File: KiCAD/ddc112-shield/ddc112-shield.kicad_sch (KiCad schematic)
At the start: 24 parts, among them J1 Power, J2 Digital/PWM, J3 Analog, J4 Digital/PWM, J5 Conn_02x03_Odd_Even, U2 REF3040, U3 OPA350, Y1 10MHZ

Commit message: working on schematic
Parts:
- removed C7: 0.1uF, symbol Device:C_Small
- removed Y1: 10MHZ, Oscillator:Oscillator_DIP-8, symbol Oscillator:CXO_DIP8
- added JP1: JPR2, symbol Jumper:Jumper_2_Bridged
- added R5, R6: 10k, symbol Device:R_US
- added U4, U5: 74AHC1G86, symbol 74xGxx:74AHC1G86
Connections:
- net *9: no longer J2.9 (Pin_9)
- net GND: now also U4.3 (GND), U5.3 (GND)
- net VCC: now also U4.5 (VCC), U5.5 (VCC)
- net at U1.10 (CLK): now also U4.4
- net at U1.9 (CONV): now also U5.4
- net *6 renamed OC0A/6
- net OC0A/6: now also U4.1
- new net: R6.2, U4.2
- new net: R5.2, U5.2
- new net OC1A/9: J2.9 (Pin_9), U5.1

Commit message: initial schematic; test software
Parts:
- removed J5: Conn_02x03_Odd_Even, symbol Connector_Generic:Conn_02x03_Odd_Even
- removed JP1: JPR2, symbol Jumper:Jumper_2_Bridged
- removed R3, R4, R5, R6: 10k, symbol Device:R_US
- removed U4, U5: 74AHC1G86, symbol 74xGxx:74AHC1G86
- added C12, C13: 0.33uF, Capacitor_SMD:C_0805_2012Metric_Pad1.18x1.45mm_HandSolder, symbol Device:C_Small
- added C14, C7: 0.1uF, Capacitor_SMD:C_0805_2012Metric_Pad1.18x1.45mm_HandSolder, symbol Device:C_Small
- added J5, J6: Conn_01x02, Connector_PinHeader_2.54mm:PinHeader_1x02_P2.54mm_Vertical, symbol Connector_Generic:Conn_01x02
- added J7: Screw_Terminal_01x02, TerminalBlock:TerminalBlock_MaiXu_MX126-5.0-02P_1x02_P5.00mm, symbol Connector:Screw_Terminal_01x02
- added U4, U5: L78L05_SOT89, Package_TO_SOT_SMD:SOT-89-3, symbol Regulator_Linear:L78L05_SOT89
- C1, C10, C11, C2, C3, C4, C5, C6, C8, C9: footprint (none) -> Capacitor_SMD:C_0805_2012Metric_Pad1.18x1.45mm_HandSolder
- R1: footprint (none) -> Resistor_SMD:R_0805_2012Metric_Pad1.20x1.40mm_HandSolder
- R2: value 10k -> 0R; footprint (none) -> Resistor_SMD:R_0805_2012Metric_Pad1.20x1.40mm_HandSolder
- U1: value ~ -> DDC112; footprint (none) -> Package_SO:SOIC-28W_7.5x17.9mm_P1.27mm
- U3: footprint (none) -> Package_SO:SOIC-8_3.9x4.9mm_P1.27mm
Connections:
- net *5 is gone; now on net PD5: J4.3 (Pin_3)
- net 7 is gone; now on net PD7: J4.1 (Pin_1)
- net A0 is gone; now on net PC0/ADC0: J3.1 (Pin_1)
- net A1 is gone; now on net PC1/ADC1: J3.2 (Pin_2)
- net A2 is gone; now on net PC2/ADC2: J3.3 (Pin_3)
- net OC0A/6 is gone; now on net PD6/OC0A: J4.2 (Pin_2)
- net OC1A/9 is gone; now on net PB1/OC1A: J2.9 (Pin_9)
- net +5VA: now also C7.1, U4.1 (OUT)
- net Earth: now also R2.2, C12.2, C7.2, J5.2 (Pin_2), J6.2 (Pin_2), U4.2 (GND)
- net GND: now also R2.1, C13.2, C14.2, J7.2 (Pin_2), U5.2 (GND)
- net MISO/12: no longer J2.6 (Pin_6)
- net MOSI/11: no longer J2.7 (Pin_7)
- net VCC: now also C14.1, U5.1 (OUT); no longer J1.8 (Pin_8), R2.2
- net PC1/ADC1: now reaches U1.19 (RANGE1)
- net PC2/ADC2: now reaches U1.20 (RANGE2)
- net PC0/ADC0: now reaches U1.18 (RANGE0)
- net PC0/ADC0: no longer R2.1
- net at U1.1 (IN1): now also J5.1 (Pin_1)
- net PD6/OC0A: now reaches U1.10 (CLK)
- net at U1.28 (IN2): now also J6.1 (Pin_1)
- net PD5: now reaches U1.8 (TEST)
- net PB1/OC1A: now reaches U1.9 (CONV)
- net *3 renamed PD3
- net *9 renamed PD7
- net 2 renamed PD2
- net 4 renamed PD4
- net 8 renamed PB0
- net PB0: now also U1.12 (~{DXMIT})
- net A3 renamed PC3/ADC3
- net RX/0 renamed PD0/TXD
- net SCLK/13 renamed PB5/SCLK
- net SCL/A5 renamed PC5/SCL/ADC5
- net SDA/A4 renamed PC4/SDA/ADC4
- net SS/10 renamed PB2/SS
- net PB2/SS: no longer U1.12 (~{DXMIT})
- net TX/1 renamed PD1/TXD
- new net PB3/MOSI: J2.7 (Pin_7)
- new net PB4/MISO: J2.6 (Pin_6)
- new net VBUS: C12.1, C13.1, J7.1 (Pin_1), U4.3 (IN), U5.3 (IN)
- new net Vin: J1.8 (Pin_8)
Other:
- note added: "9V POWER"
- note added: "BU BOTLAB"
- note added: "PHOTODIODE INPUTS"
- note added: "Photodiode ADC (DDC112) Evaluation board (Arduino shield)"
- note removed: "* Indicates a PWM-capable pin"

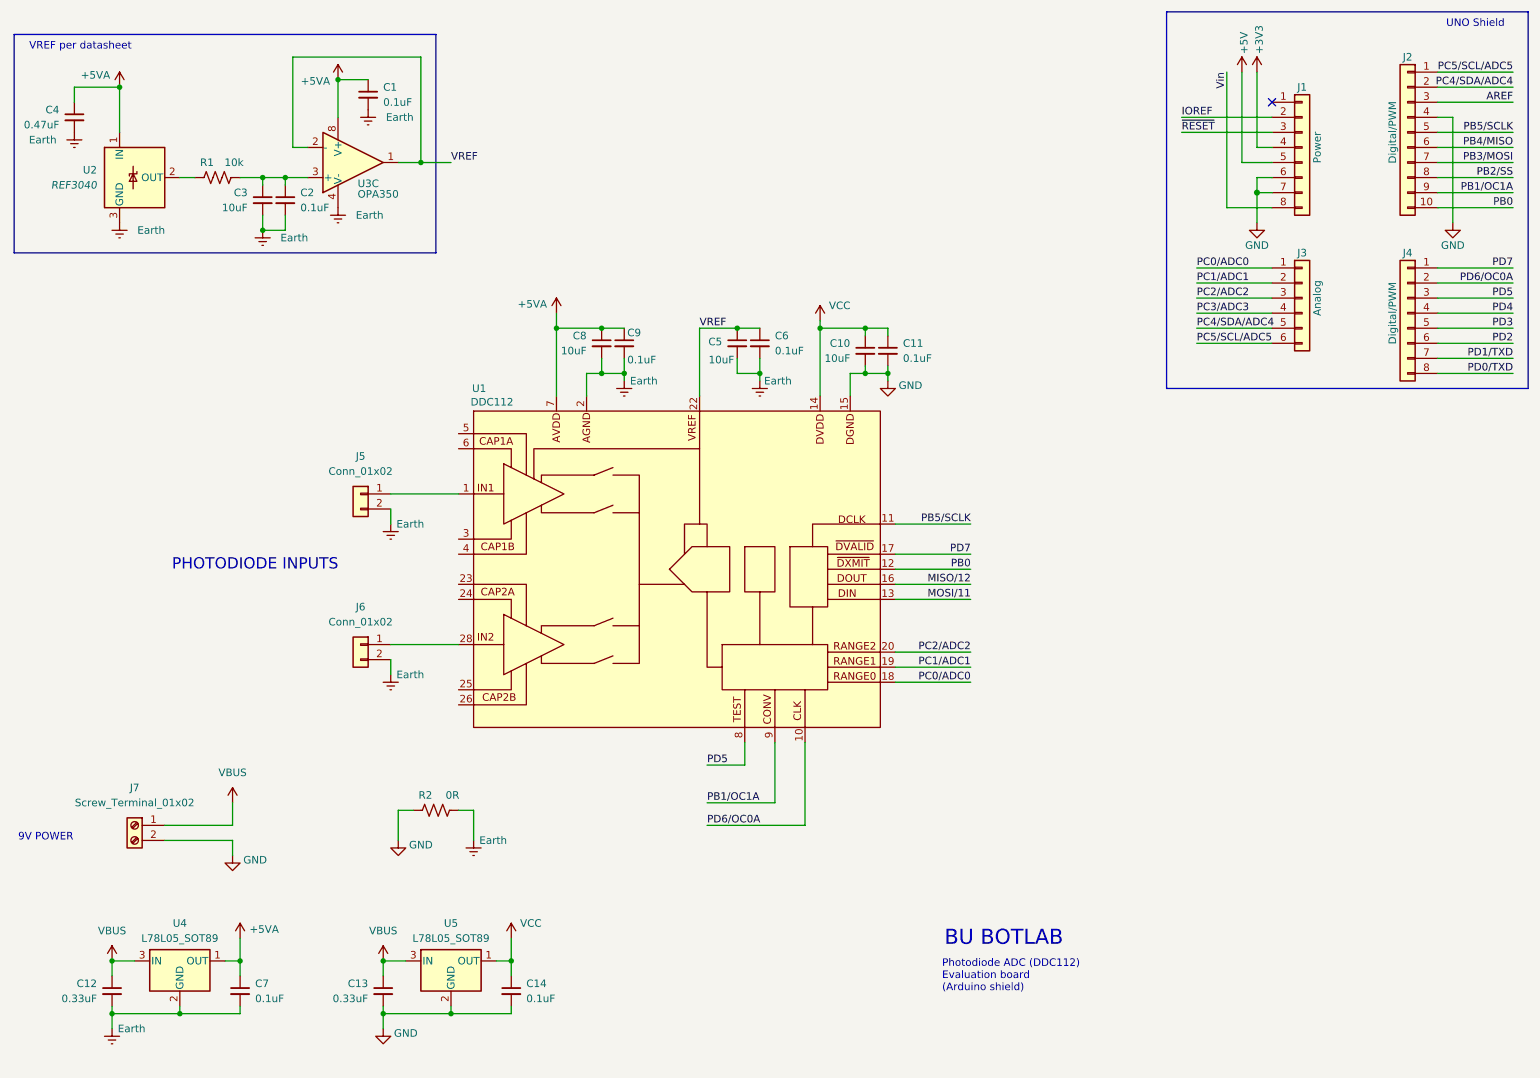
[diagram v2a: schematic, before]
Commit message: starting on LED driver
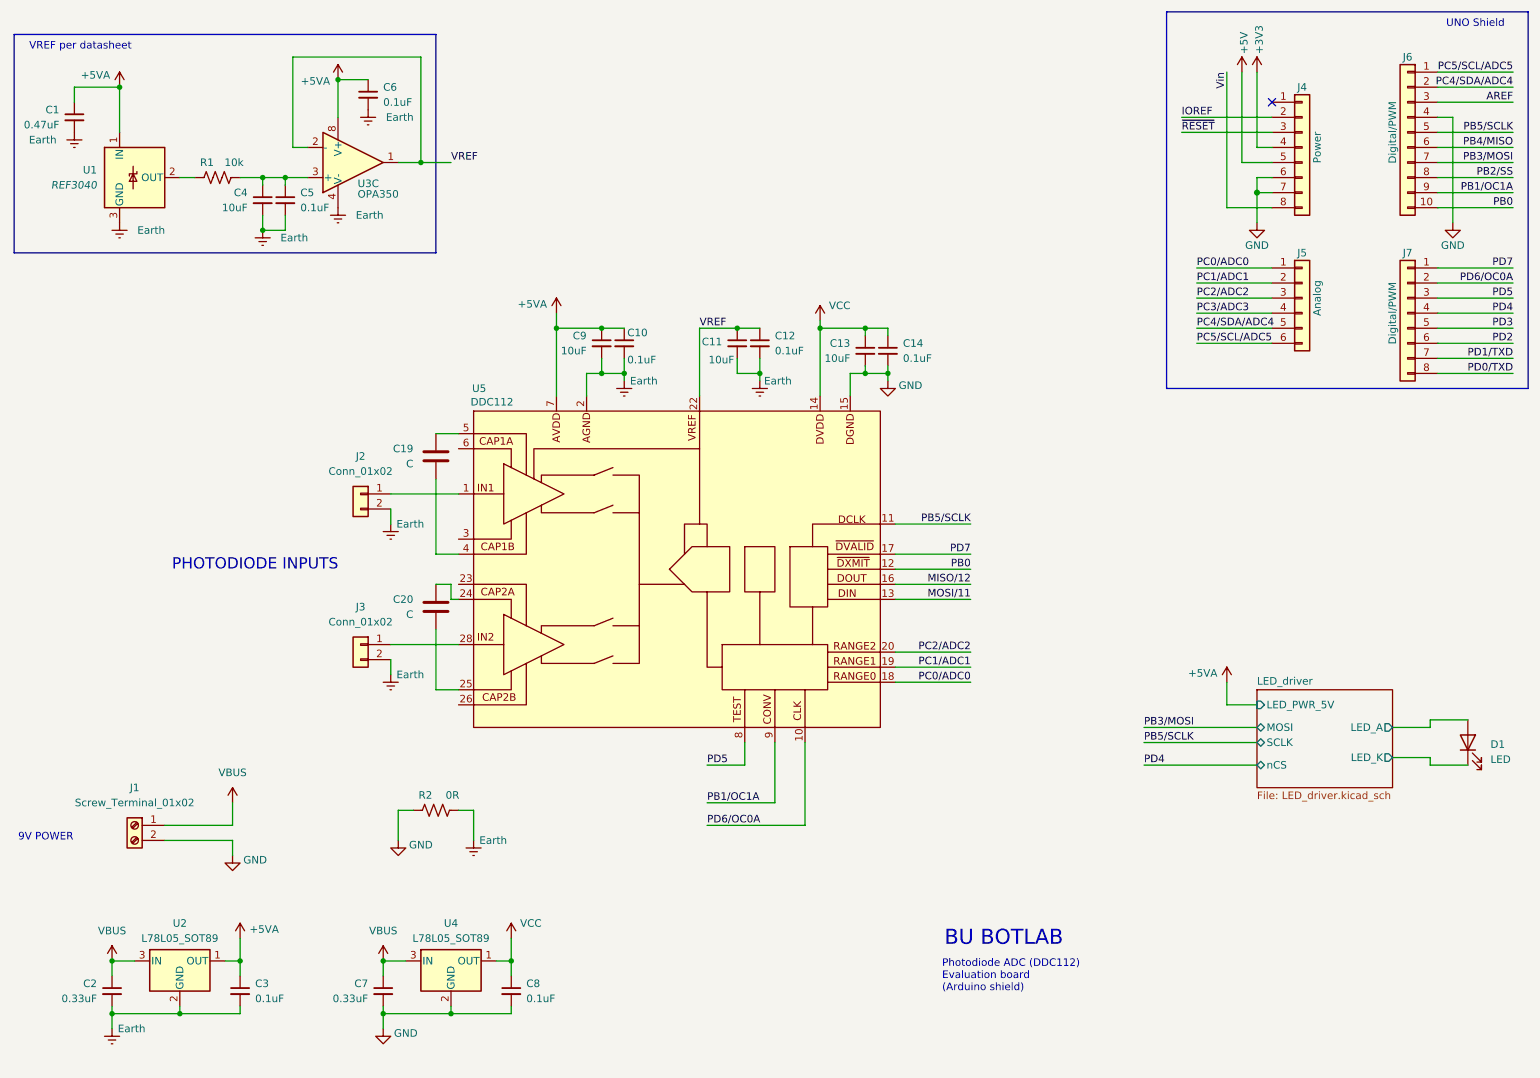
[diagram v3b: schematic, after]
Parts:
- added C19, C20: C, Capacitor_SMD:C_0805_2012Metric_Pad1.18x1.45mm_HandSolder, symbol Device:C
- added D1: LED, Connector_PinHeader_2.54mm:PinHeader_1x02_P2.54mm_Vertical, symbol Device:LED
- renumbered C4 to C1, C9 to C10, C5 to C11, C6 to C12, C10 to C13, C11 to C14, C12 to C2, C7 to C3, C3 to C4, C2 to C5, C1 to C6, C13 to C7, C14 to C8, C8 to C9, J7 to J1, J5 to J2, J6 to J3, J1 to J4, J3 to J5, J2 to J6, J4 to J7, U2 to U1, U4 to U2, U5 to U4, U1 to U5
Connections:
- net at U5.24 (CAP2A): now also C20.1
- net at U5.25 (CAP2B): now also C20.2
- net at U5.4 (CAP1B): now also C19.2
- net at U5.5 (CAP1A): now also C19.1
- new net LED_driver/LED_A: D1.2 (A)
- new net LED_driver/LED_K: D1.1 (K)
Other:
- added sheet LED_driver (LED_driver.kicad_sch)

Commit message: woring on LED driver
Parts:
- added D2, D3: LED, Connector_PinHeader_2.54mm:PinHeader_1x02_P2.54mm_Vertical, symbol Device:LED
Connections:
- net LED_driver/LED_K: now also D2.1 (K), D3.1 (K)
- net LED_driver/LED_A renamed LED_driver/LED_1
- new net LED_driver/LED_2: D2.2 (A)
- new net LED_driver/LED_3: D3.2 (A)
- no-connect marks 1 -> 2
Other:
- sheet LED_driver ports: added LED_1, LED_2, LED_3, LED_4, SCL, SDA; removed LED_A, MOSI, SCLK, nCS
- moved on the sheet: D1

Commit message: LED driver schematic complete?
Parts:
- added R8, R9: 4.7k, Resistor_SMD:R_0805_2012Metric_Pad1.20x1.40mm_HandSolder, symbol Device:R_US
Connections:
- net MISO/12 is gone; now on net PB4/MISO: U5.16 (DOUT)
- net MOSI/11 is gone; now on net PB3/MOSI: U5.13 (DIN)
- net PC4/SDA/ADC4: now also R9.2
- net PC5/SCL/ADC5: now also R8.2
- net VCC: now also R8.1, R9.1
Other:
- moved on the sheet: D1, D2, D3
